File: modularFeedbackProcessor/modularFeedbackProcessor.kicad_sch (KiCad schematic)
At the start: 103 parts, among them J1 Input, J10 Output, J2 Feedback, J4 Eurorack_Power_16pin_Unshroud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, J5 DryWet, J6 Rate, J7 EffectsRouteIn, J8 EffectsRouteOut, J9 EffectsDryWet, Q1 Q_PMOS_GDS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

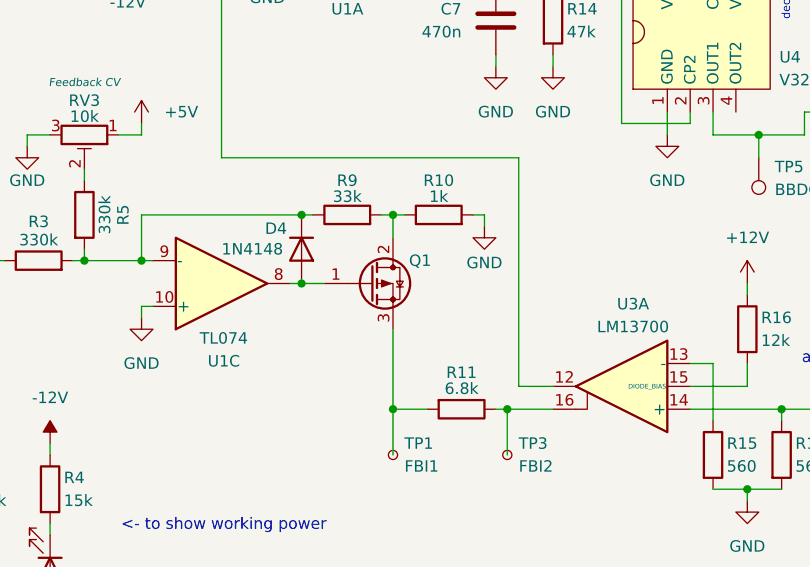
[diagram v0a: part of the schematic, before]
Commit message: Fixed error with Q1. Drain/source were swapped. Unfortunately the PCB will not receive such fixing before it arrives.
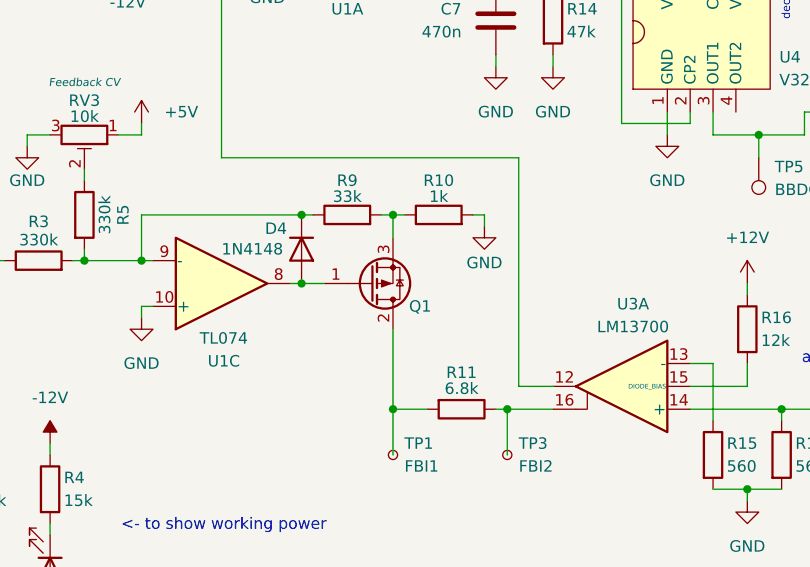
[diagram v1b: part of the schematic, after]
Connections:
- net at R10.1, R9.2: now also Q1.3 (S); no longer Q1.2 (D)
- net at R11.2, TP1.1: now also Q1.2 (D); no longer Q1.3 (S)
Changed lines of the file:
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@@
 		(lib_id "Transistor_FET:Q_PMOS_GDS")
 		(at 78.74 118.11 0)
+		(mirror x)
 		(unit 1)
 		(body_style 1)
@@
 		(dnp no)
 		(property "Reference" "Q1"
-			(at 83.058 115.57 0)
+			(at 83.058 120.65 0)
 			(show_name no)
 			(do_not_autoplace no)
@@
 		)
 		(property "Value" "Q_PMOS_GDS"
-			(at 85.09 119.3799 0)
+			(at 85.09 116.8401 0)
 			(hide yes)
 			(show_name no)
@@
 		)
 		(property "Footprint" "Package_TO_SOT_THT:TO-220-3_Vertical"
-			(at 83.82 115.57 0)
+			(at 83.82 120.65 0)
 			(hide yes)
 			(show_name no)

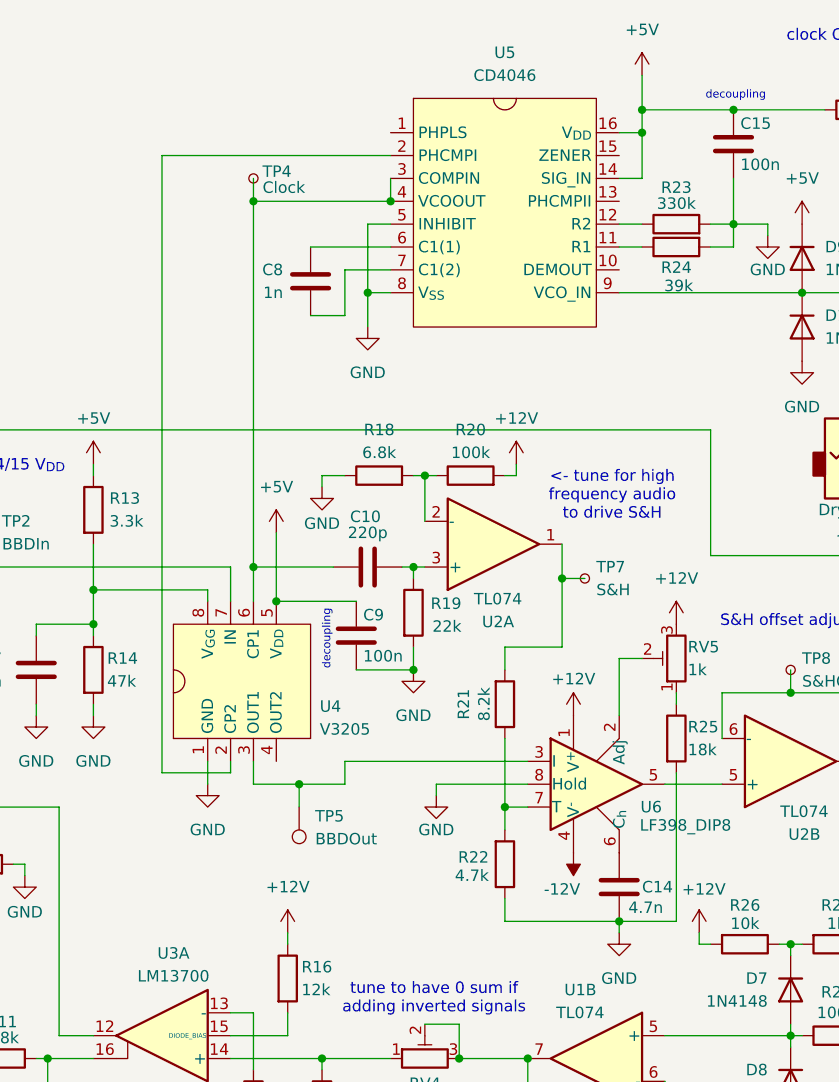
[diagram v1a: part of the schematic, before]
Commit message: Added DC blocking capacitor in S&H. Changed S&H sampling cap to 10n
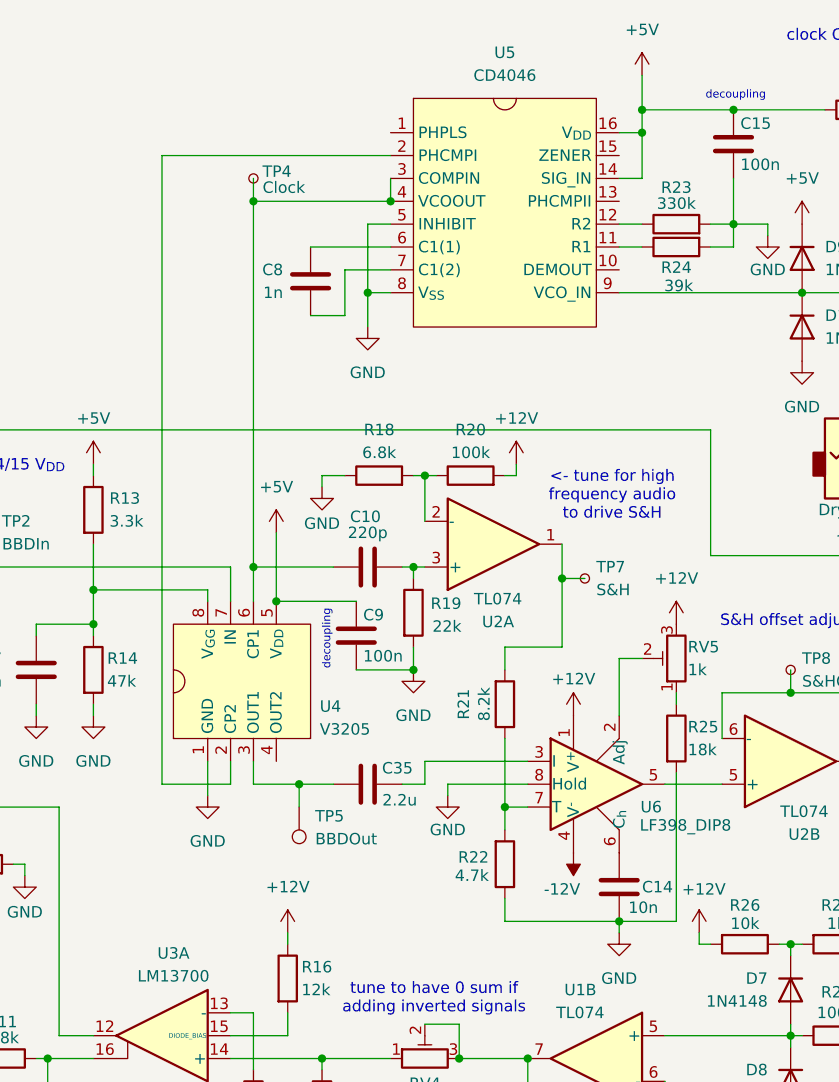
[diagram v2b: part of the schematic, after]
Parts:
- added C35: 2.2u, symbol Device:C
- C14: value 4.7n -> 10n
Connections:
- net at TP5.1, U4.3 (OUT1): now also C35.2; no longer U6.3 (I)
- new net: C35.1, U6.3 (I)
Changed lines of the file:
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@@
 	)
 	(junction
-		(at 121.92 101.6)
-		(diameter 0)
-		(color 0 0 0 0)
-	)
-	(junction
 		(at 177.8 46.99)
 		(diameter 0)
@@
 	)
 	(junction
+		(at 121.92 101.6)
+		(diameter 0)
+		(color 0 0 0 0)
+	)
+	(junction
 		(at 176.53 119.38)
 		(diameter 0)
@@
 	(wire
 		(pts
-			(xy 106.68 100.33) (xy 114.3 100.33)
+			(xy 106.68 101.6) (xy 114.3 101.6)
 		)
 		(stroke
@@
 	(wire
 		(pts
+			(xy 133.35 101.6) (xy 135.89 101.6)
+		)
+		(stroke
+			(width 0)
+			(type default)
+		)
+	)
+	(wire
+		(pts
 			(xy 120.65 118.11) (xy 120.65 119.38)
 		)
@@
 	(wire
 		(pts
+			(xy 135.89 101.6) (xy 135.89 99.06)
+		)
+		(stroke
+			(width 0)
+			(type default)
+		)
+	)
+	(wire
+		(pts
 			(xy 162.56 138.43) (xy 151.13 138.43)
 		)
@@
 	(wire
 		(pts
-			(xy 144.78 67.31) (xy 146.05 67.31)
+			(xy 135.89 99.06) (xy 147.32 99.06)
 		)
 		(stroke
@@
 	(wire
 		(pts
-			(xy 123.19 49.53) (xy 127 49.53)
+			(xy 144.78 67.31) (xy 146.05 67.31)
 		)
 		(stroke
@@
 	(wire
 		(pts
-			(xy 127 101.6) (xy 127 99.06)
+			(xy 123.19 49.53) (xy 127 49.53)
 		)
 		(stroke
@@
 	(wire
 		(pts
-			(xy 137.16 101.6) (xy 147.32 101.6)
+			(xy 138.43 101.6) (xy 147.32 101.6)
 		)
 		(stroke
@@
 	(wire
 		(pts
-			(xy 127 99.06) (xy 147.32 99.06)
-		)
-		(stroke
-			(width 0)
-			(type default)
-		)
-	)
-	(wire
-		(pts
 			(xy 130.81 182.88) (xy 130.81 181.61)
 		)
@@
 	(wire
 		(pts
-			(xy 114.3 100.33) (xy 114.3 99.06)
+			(xy 114.3 101.6) (xy 114.3 99.06)
 		)
 		(stroke
@@
 	(wire
 		(pts
-			(xy 111.76 99.06) (xy 111.76 101.6)
+			(xy 111.76 99.06) (xy 111.76 102.87)
 		)
 		(stroke
@@
 	(wire
 		(pts
-			(xy 106.68 31.75) (xy 106.68 100.33)
+			(xy 106.68 31.75) (xy 106.68 101.6)
 		)
 		(stroke
@@
 	(wire
 		(pts
-			(xy 121.92 101.6) (xy 127 101.6)
+			(xy 121.92 101.6) (xy 125.73 101.6)
 		)
 		(stroke
@@
 	(wire
 		(pts
-			(xy 137.16 101.6) (xy 137.16 102.87)
+			(xy 138.43 101.6) (xy 138.43 102.87)
 		)
 		(stroke
@@
 	(symbol
 		(lib_id "power:GND")
-		(at 137.16 102.87 0)
+		(at 138.43 102.87 0)
 		(unit 1)
 		(body_style 1)
@@
 		(dnp no)
 		(property "Reference" "#PWR043"
-			(at 137.16 109.22 0)
+			(at 138.43 109.22 0)
 			(hide yes)
 			(show_name no)
@@
 		)
 		(property "Value" "GND"
-			(at 137.16 106.68 0)
+			(at 138.43 106.68 0)
 			(show_name no)
 			(do_not_autoplace no)
@@
 		)
 		(property "Footprint" ""
-			(at 137.16 102.87 0)
+			(at 138.43 102.87 0)
 			(hide yes)
 			(show_name no)
@@
 		)
 		(property "Datasheet" ""
-			(at 137.16 102.87 0)
+			(at 138.43 102.87 0)
 			(hide yes)
 			(show_name no)
@@
 		)
 		(property "Description" "Power symbol creates a global label with name \"GND\" , ground"
-			(at 137.16 102.87 0)
+			(at 138.43 102.87 0)
 			(hide yes)
 			(show_name no)
@@
 	(symbol
 		(lib_id "power:GND")
-		(at 111.76 101.6 0)
+		(at 111.76 102.87 0)
 		(unit 1)
 		(body_style 1)
@@
 		(fields_autoplaced yes)
 		(property "Reference" "#PWR032"
-			(at 111.76 107.95 0)
+			(at 111.76 109.22 0)
 			(hide yes)
 			(show_name no)
@@
 		)
 		(property "Value" "GND"
-			(at 111.76 106.68 0)
+			(at 111.76 107.95 0)
 			(show_name no)
 			(do_not_autoplace no)
@@
 		)
 		(property "Footprint" ""
-			(at 111.76 101.6 0)
+			(at 111.76 102.87 0)
 			(hide yes)
 			(show_name no)
@@
 		)
 		(property "Datasheet" ""
-			(at 111.76 101.6 0)
+			(at 111.76 102.87 0)
 			(hide yes)
 			(show_name no)
@@
 		)
 		(property "Description" "Power symbol creates a global label with name \"GND\" , ground"
-			(at 111.76 101.6 0)
+			(at 111.76 102.87 0)
 			(hide yes)
 			(show_name no)
@@
 			)
 		)
-		(property "Value" "4.7n"
+		(property "Value" "10n"
 			(at 158.496 115.316 0)
 			(show_name no)
@@
 					(unit 1)
 				)
+			)
+		)
+	)
+	(symbol
+		(lib_id "Device:C")
+		(at 129.54 101.6 270)
+		(unit 1)
+		(body_style 1)
+		(exclude_from_sim no)
+		(in_bom yes)
+		(on_board yes)
+		(in_pos_files yes)
+		(dnp no)
+		(property "Reference" "C35"
+			(at 132.842 99.822 90)
+			(show_name no)
+			(do_not_autoplace no)
+			(effects
+				(font
+					(size 1.27 1.27)
+				)
+			)
+		)
+		(property "Value" "2.2u"
+			(at 133.096 103.378 90)
+			(show_name no)
+			(do_not_autoplace no)
+			(effects
+				(font
+					(size 1.27 1.27)
+				)
+			)
+		)
+		(property "Footprint" ""
+			(at 125.73 102.5652 0)
+			(hide yes)
+			(show_name no)
+			(do_not_autoplace no)
+			(effects
+				(font
+					(size 1.27 1.27)
+				)
+			)
+		)
+		(property "Datasheet" ""
+			(at 129.54 101.6 0)
+			(hide yes)
+			(show_name no)
+			(do_not_autoplace no)
+			(effects
+				(font
+					(size 1.27 1.27)
+				)
+			)
+		)
+		(property "Description" "Unpolarized capacitor"
+			(at 129.54 101.6 0)
+			(hide yes)
+			(show_name no)
+			(do_not_autoplace no)
+			(effects
+				(font
+					(size 1.27 1.27)
+				)
+			)
+		)
+		(pin "1"
+		)
+		(pin "2"
+		)
+		(instances
+			(project "modularFeedbackProcessor"
+				(path "/a81d404d-f7d3-4fe2-a135-d74fc6d7b6a7"
+					(reference "C35")
+					(unit 1)
+				)

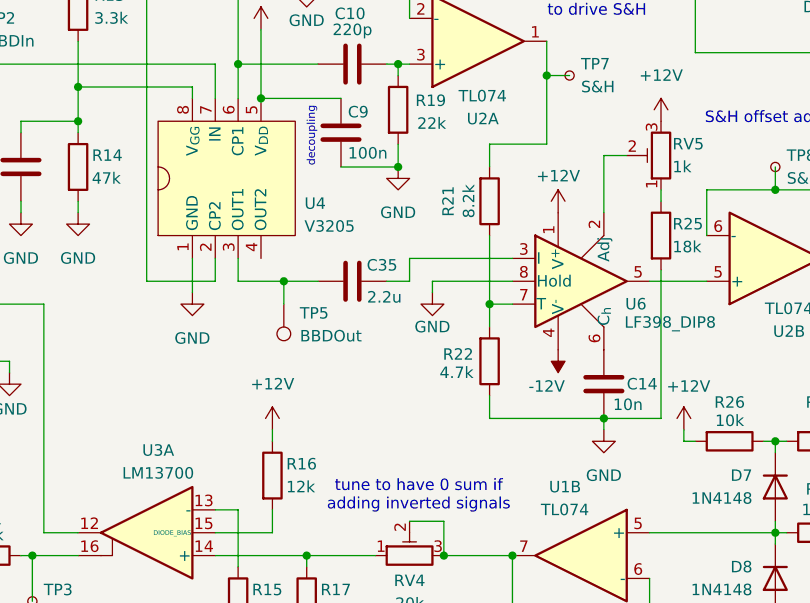
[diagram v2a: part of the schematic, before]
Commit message: Added resistors for DC blocking cap. Added decoupling caps for LF398.
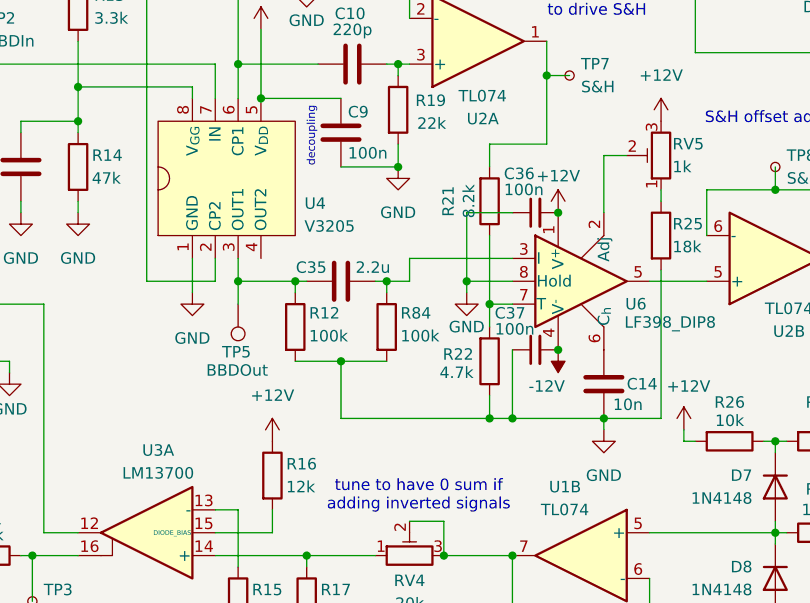
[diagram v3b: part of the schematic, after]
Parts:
- added C36, C37: 100n, symbol Device:C_Small
- added R12, R84: 100k, symbol Device:R
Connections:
- net +12V: now also C36.2
- net -12V: now also C37.2
- net GND: now also C36.1, C37.1, R12.2, R84.2
- net at C35.2, TP5.1, U4.3 (OUT1): now also R12.1
- net at C35.1, U6.3 (I): now also R84.1
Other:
- moved on the sheet: C35, TP5

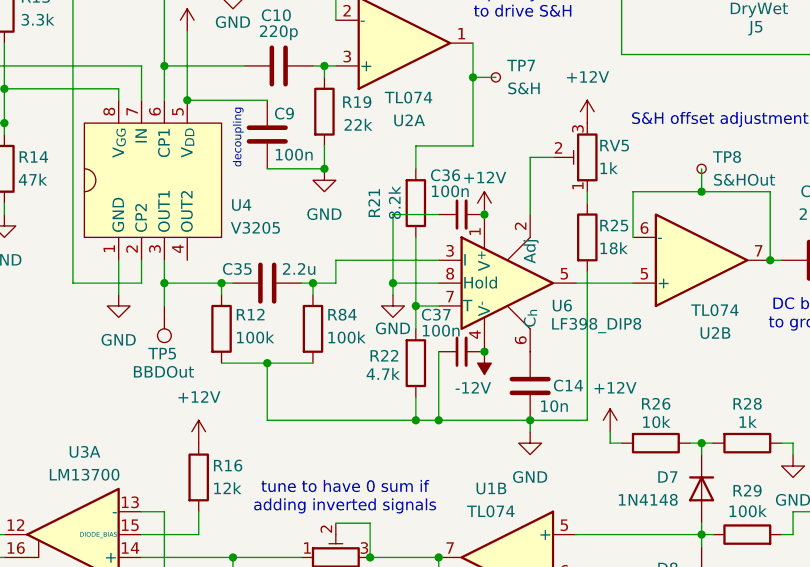
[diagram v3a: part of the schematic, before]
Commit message: swapped pins 7 and 8 of LF398
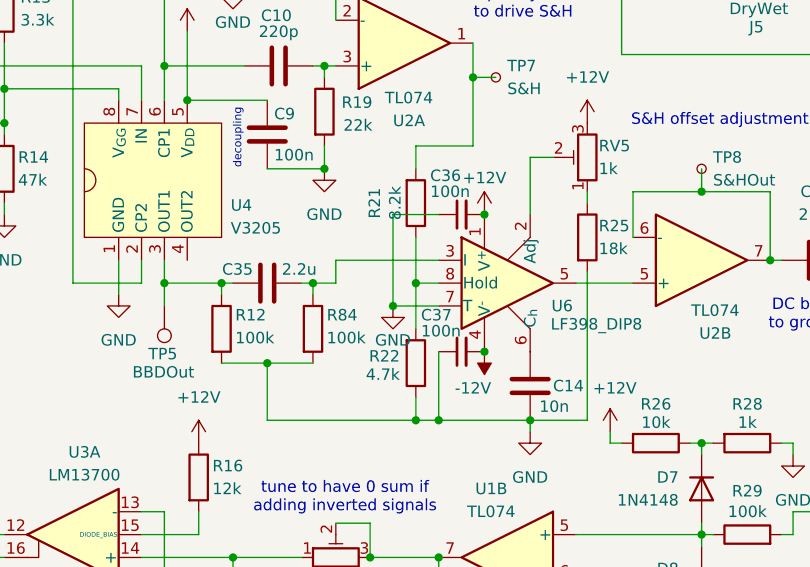
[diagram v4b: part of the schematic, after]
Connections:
- net GND: now also U6.7 (T); no longer U6.8 (Hold)
- net at R21.1, R22.2: now also U6.8 (Hold); no longer U6.7 (T)
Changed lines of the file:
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@@
 	)
 	(junction
-		(at 144.78 104.14)
-		(diameter 0)
-		(color 0 0 0 0)
-	)
-	(junction
 		(at 215.9 31.75)
 		(diameter 0)
@@
 	)
 	(junction
+		(at 142.24 104.14)
+		(diameter 0)
+		(color 0 0 0 0)
+	)
+	(junction
 		(at 171.45 176.53)
 		(diameter 0)
@@
 	)
 	(junction
+		(at 144.78 101.6)
+		(diameter 0)
+		(color 0 0 0 0)
+	)
+	(junction
 		(at 152.4 93.98)
 		(diameter 0)
@@
 	)
 	(junction
-		(at 142.24 101.6)
-		(diameter 0)
-		(color 0 0 0 0)
-	)
-	(junction
 		(at 195.58 99.06)
 		(diameter 0)
@@
 	(wire
 		(pts
+			(xy 142.24 104.14) (xy 147.32 104.14)
+		)
+		(stroke
+			(width 0)
+			(type default)
+		)
+	)
+	(wire
+		(pts
 			(xy 87.63 73.66) (xy 87.63 77.47)
 		)
@@
 	(wire
 		(pts
-			(xy 142.24 101.6) (xy 147.32 101.6)
-		)
-		(stroke
-			(width 0)
-			(type default)
-		)
-	)
-	(wire
-		(pts
 			(xy 167.64 39.37) (xy 170.18 39.37)
 		)
@@
 	(wire
 		(pts
+			(xy 144.78 101.6) (xy 147.32 101.6)
+		)
+		(stroke
+			(width 0)
+			(type default)
+		)
+	)
+	(wire
+		(pts
 			(xy 170.18 179.07) (xy 171.45 179.07)
 		)
@@
 	(wire
 		(pts
-			(xy 147.32 93.98) (xy 142.24 93.98)
+			(xy 142.24 93.98) (xy 147.32 93.98)
 		)
 		(stroke
@@
 	(wire
 		(pts
-			(xy 171.45 173.99) (xy 171.45 176.53)
+			(xy 144.78 101.6) (xy 144.78 106.68)
 		)
 		(stroke
@@
 	(wire
 		(pts
-			(xy 234.95 115.57) (xy 234.95 116.84)
+			(xy 171.45 173.99) (xy 171.45 176.53)
 		)
 		(stroke
@@
 	(wire
 		(pts
-			(xy 207.01 34.29) (xy 218.44 34.29)
+			(xy 234.95 115.57) (xy 234.95 116.84)
 		)
 		(stroke
@@
 	(wire
 		(pts
-			(xy 151.13 186.69) (xy 152.4 186.69)
+			(xy 207.01 34.29) (xy 218.44 34.29)
 		)
 		(stroke
@@
 	(wire
 		(pts
-			(xy 173.99 39.37) (xy 173.99 40.64)
+			(xy 151.13 186.69) (xy 152.4 186.69)
 		)
 		(stroke
@@
 	(wire
 		(pts
-			(xy 144.78 96.52) (xy 144.78 104.14)
+			(xy 173.99 39.37) (xy 173.99 40.64)
 		)
 		(stroke
@@
 	(wire
 		(pts
-			(xy 142.24 93.98) (xy 142.24 101.6)
-		)
-		(stroke
-			(width 0)
-			(type default)
-		)
-	)
-	(wire
-		(pts
 			(xy 114.3 77.47) (xy 114.3 81.28)
 		)
@@
 	(wire
 		(pts
-			(xy 142.24 101.6) (xy 142.24 102.87)
+			(xy 142.24 93.98) (xy 142.24 104.14)
 		)
 		(stroke
@@
 	(wire
 		(pts
-			(xy 144.78 104.14) (xy 144.78 106.68)
+			(xy 144.78 96.52) (xy 144.78 101.6)
 		)
 		(stroke
@@
 		)
 	)
-	(wire
-		(pts
-			(xy 144.78 104.14) (xy 147.32 104.14)
-		)
-		(stroke
-			(width 0)
-			(type default)
-		)
-	)
 	(label "in"
 		(at 25.4 72.39 0)
@@
 	(symbol
 		(lib_id "power:GND")
-		(at 142.24 102.87 0)
+		(at 142.24 104.14 0)
 		(unit 1)
 		(body_style 1)
@@
 		(dnp no)
 		(property "Reference" "#PWR043"
-			(at 142.24 109.22 0)
+			(at 142.24 110.49 0)
 			(hide yes)
 			(show_name no)
@@
 		)
 		(property "Value" "GND"
-			(at 142.24 106.68 0)
+			(at 142.24 107.95 0)
 			(show_name no)
 			(do_not_autoplace no)
@@
 		)
 		(property "Footprint" ""
-			(at 142.24 102.87 0)
+			(at 142.24 104.14 0)
 			(hide yes)
 			(show_name no)
@@
 		)
 		(property "Datasheet" ""
-			(at 142.24 102.87 0)
+			(at 142.24 104.14 0)
 			(hide yes)
 			(show_name no)
@@
 		)
 		(property "Description" "Power symbol creates a global label with name \"GND\" , ground"
-			(at 142.24 102.87 0)
+			(at 142.24 104.14 0)
 			(hide yes)
 			(show_name no)
